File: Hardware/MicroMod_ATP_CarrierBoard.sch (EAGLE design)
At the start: 68 parts, among them J19 QWIIC_RIGHT_ANGLE, J2 JTAG, J20 QWIIC_RIGHT_ANGLE, J21 1X04_SMD_STRAIGHT_COMBO, J4 USB_A_SMT_FEMALE, J6 MICROMOD-2222-C, J8 1X04_SMD_STRAIGHT_COMBO, U5 AP7361C-33

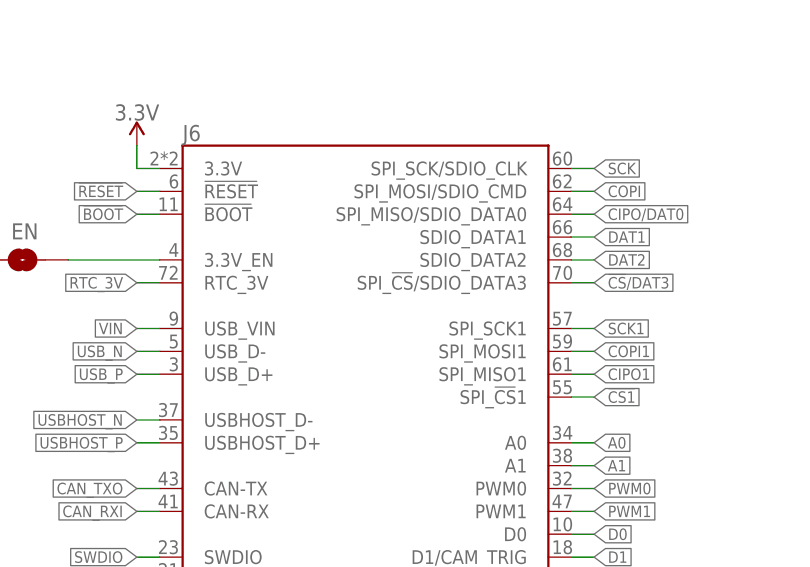
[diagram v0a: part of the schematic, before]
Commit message: Update M.2 Connector and repanelizes for production
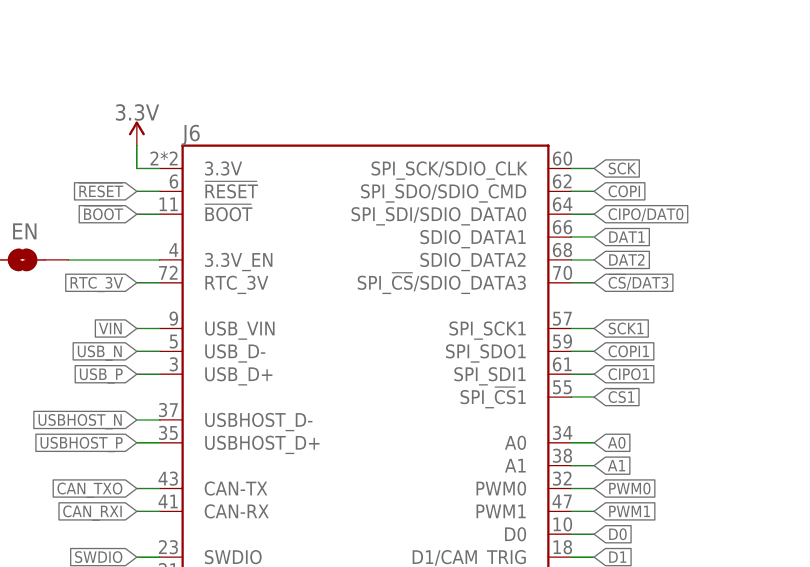
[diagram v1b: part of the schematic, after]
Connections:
- net CIPO/DAT0: now also J6.SPI_SDI/SDIO_DATA0; no longer J6.SPI_MISO/SDIO_DATA0
- net CIPO1: now also J6.SPI_SDI1; no longer J6.SPI_MISO1
- net COPI: now also J6.SPI_SDO/SDIO_CMD; no longer J6.SPI_MOSI/SDIO_CMD
- net COPI1: now also J6.SPI_SDO1; no longer J6.SPI_MOSI1
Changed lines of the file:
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@@
 <wire x1="78.74" y1="129.54" x2="81.28" y2="129.54" width="0.1524" layer="91"/>
 <label x="81.28" y="129.54" size="1.27" layer="95" xref="yes"/>
-<pinref part="J6" gate="J1" pin="SPI_MOSI/SDIO_CMD"/>
+<pinref part="J6" gate="J1" pin="SPI_SDO/SDIO_CMD"/>
 </segment>
 <segment>
@@
 <wire x1="78.74" y1="127" x2="81.28" y2="127" width="0.1524" layer="91"/>
 <label x="81.28" y="127" size="1.27" layer="95" xref="yes"/>
-<pinref part="J6" gate="J1" pin="SPI_MISO/SDIO_DATA0"/>
+<pinref part="J6" gate="J1" pin="SPI_SDI/SDIO_DATA0"/>
 </segment>
 <segment>
@@
 <wire x1="78.74" y1="111.76" x2="81.28" y2="111.76" width="0.1524" layer="91"/>
 <label x="81.28" y="111.76" size="1.27" layer="95" xref="yes"/>
-<pinref part="J6" gate="J1" pin="SPI_MOSI1"/>
+<pinref part="J6" gate="J1" pin="SPI_SDO1"/>
 </segment>
 <segment>
@@
 <wire x1="78.74" y1="109.22" x2="81.28" y2="109.22" width="0.1524" layer="91"/>
 <label x="81.28" y="109.22" size="1.27" layer="95" xref="yes"/>
-<pinref part="J6" gate="J1" pin="SPI_MISO1"/>
-</segment>
-<segment>
+<pinref part="J6" gate="J1" pin="SPI_SDI1"/>
+</segment>
+<segment>

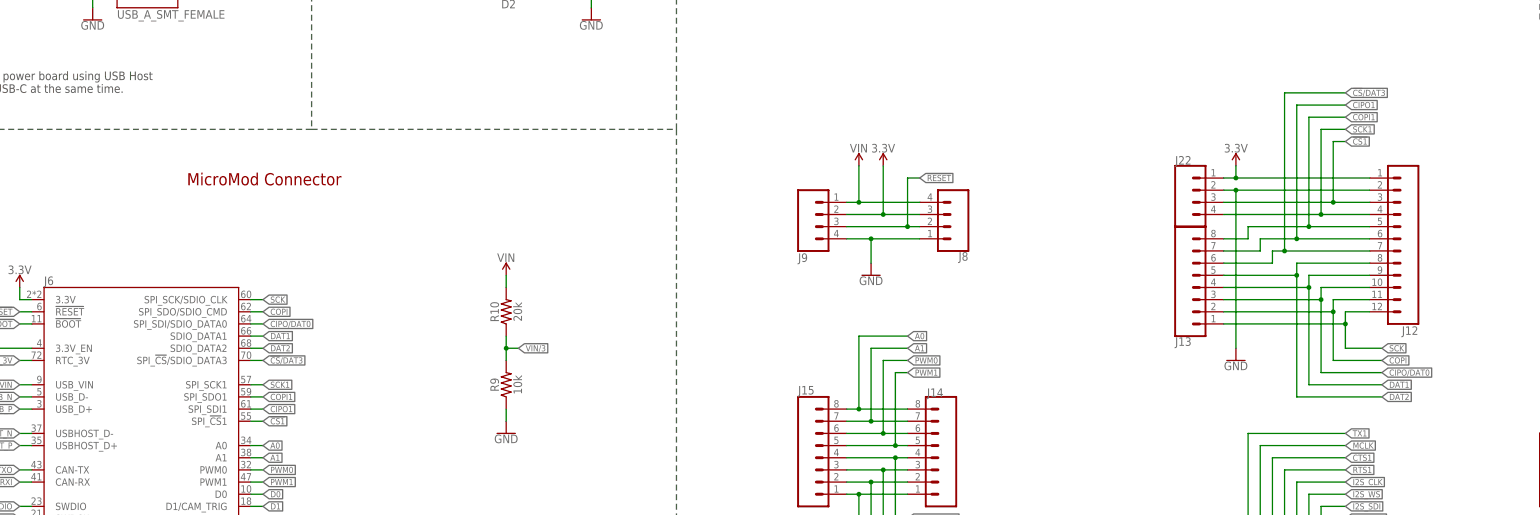
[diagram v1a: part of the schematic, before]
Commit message: Updates micromod female connector and renames nets
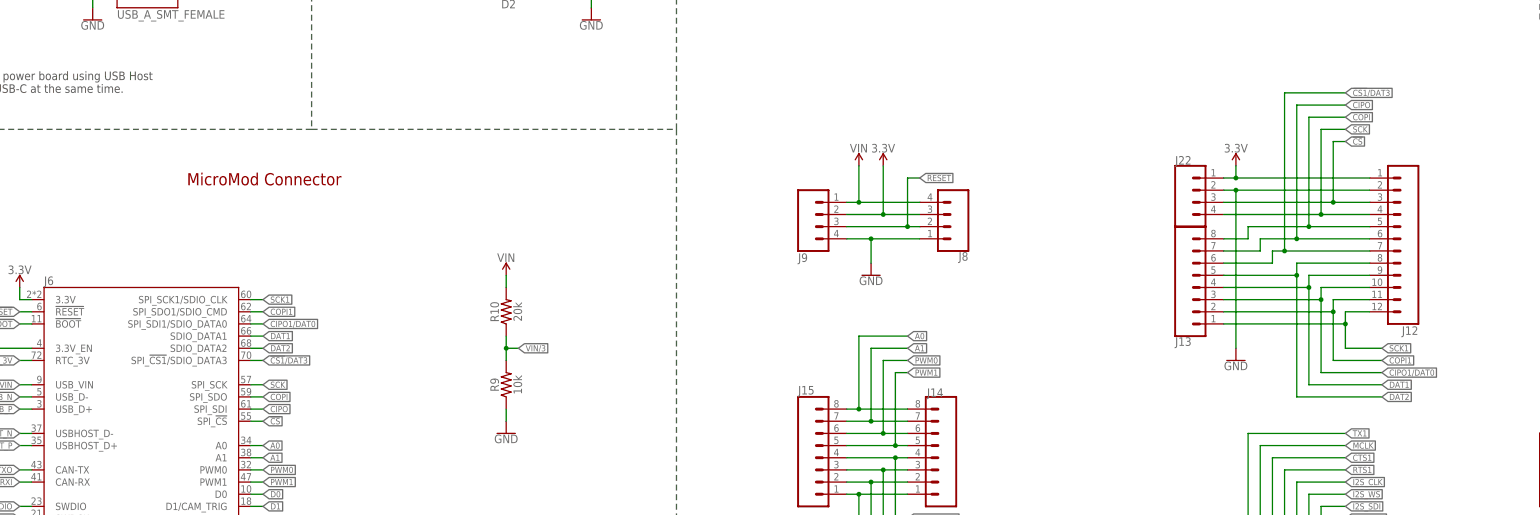
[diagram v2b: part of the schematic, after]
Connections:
- removed net !CS!/DAT3: J12.7, J13.6, J6.SPI_!CS!/SDIO_DATA3
- removed net !CS1: J12.3, J22.3, J6.SPI_!CS!1
- removed net CIPO/DAT0: J12.10, J13.3, J6.SPI_SDI/SDIO_DATA0
- removed net CIPO1: J12.6, J13.7, J6.SPI_SDI1
- new net !CS!: J12.3, J22.3, J6.SPI_!CS!
- new net !CS1!/DAT3: J12.7, J13.6, J6.SPI_!CS1!/SDIO_DATA3
- new net CIPO: J12.6, J13.7, J6.SPI_SDI
- new net CIPO1/DAT0: J12.10, J13.3, J6.SPI_SDI1/SDIO_DATA0
- net COPI: now also J12.5, J13.8, J6.SPI_SDO; no longer J12.11, J13.2, J6.SPI_SDO/SDIO_CMD
- net COPI1: now also J12.11, J13.2, J6.SPI_SDO1/SDIO_CMD; no longer J12.5, J13.8, J6.SPI_SDO1
- net SCK: now also J12.4, J22.4, J6.SPI_SCK; no longer J12.12, J13.1, J6.SPI_SCK/SDIO_CLK
- net SCK1: now also J12.12, J13.1, J6.SPI_SCK1/SDIO_CLK; no longer J12.4, J22.4, J6.SPI_SCK1

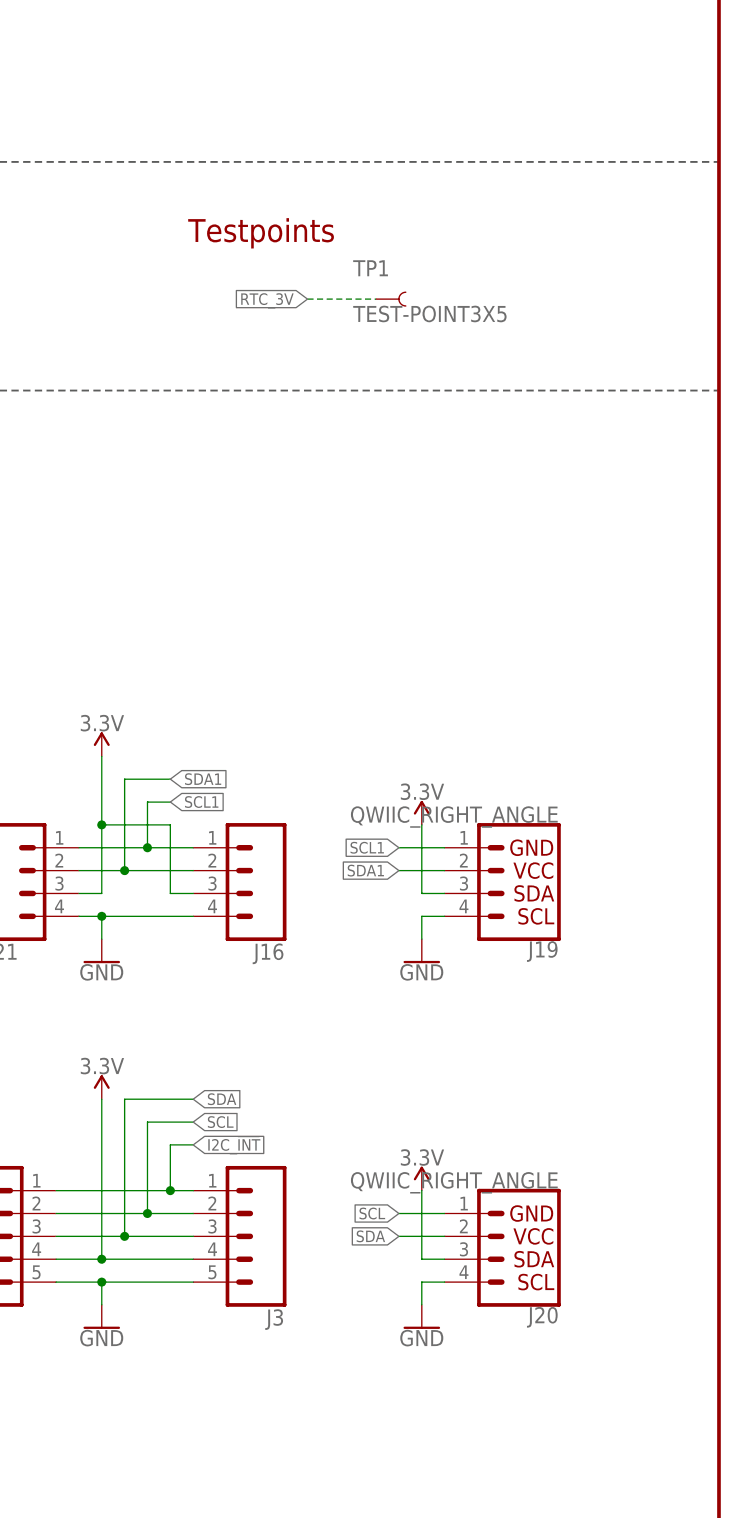
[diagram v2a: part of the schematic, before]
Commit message: Updates silk, fixes Qwiic connector wiring
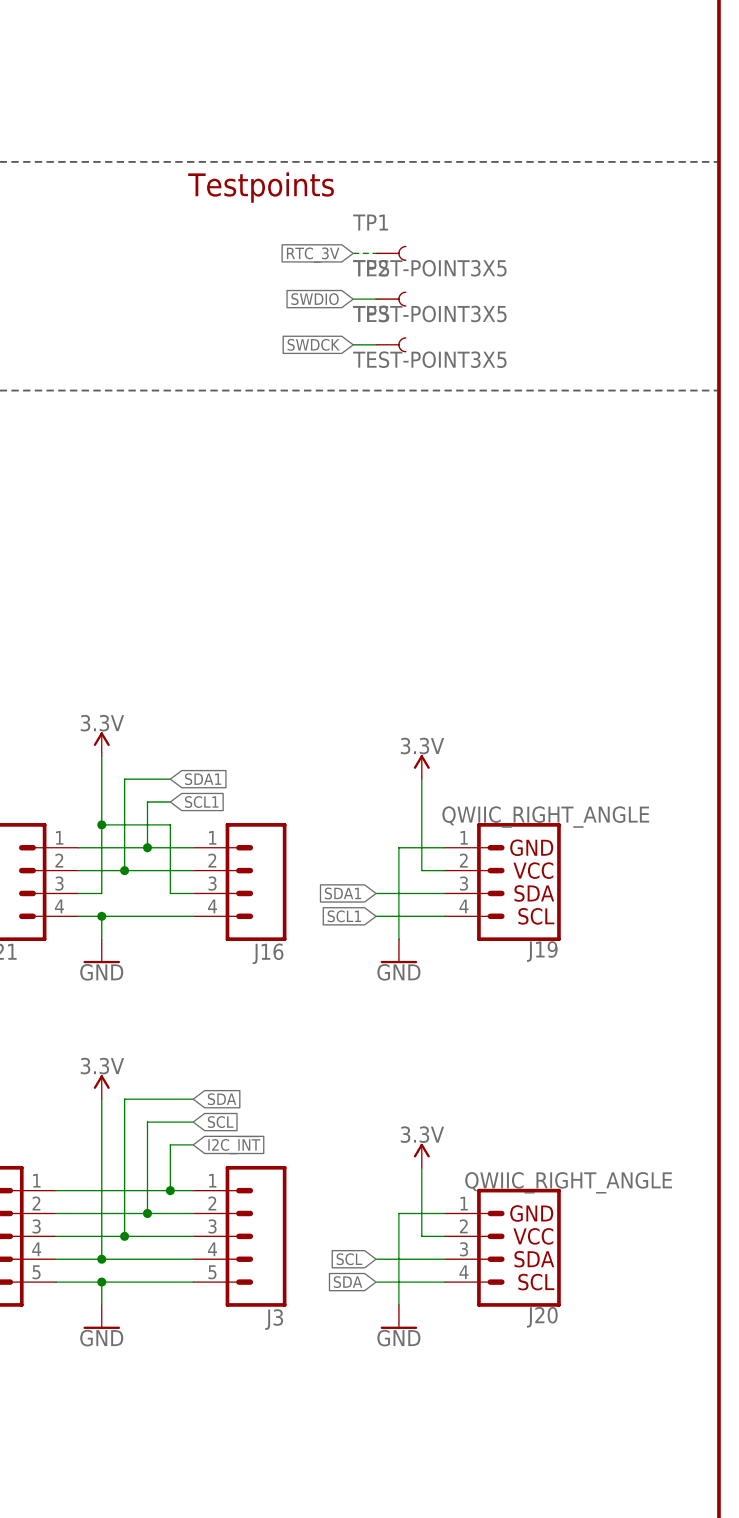
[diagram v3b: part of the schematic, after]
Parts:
- added TP2, TP3: TEST-POINT3X5, SparkFun-Connectors:TEST-POINT3X5
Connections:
- net 3.3V: now also J19.2, J20.2; no longer J19.3, J20.3
- net GND: now also J19.1, J20.1; no longer J19.4, J20.4
- net SCL: now also J20.3; no longer J20.1
- net SCL1: now also J19.4; no longer J19.1
- net SDA: now also J20.4; no longer J20.2
- net SDA1: now also J19.3; no longer J19.2
- net SWDCK: now also TP3.1
- net SWDIO: now also TP2.1
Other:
- moved on the sheet: TP1

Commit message: Updates production files
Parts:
- removed TP2, TP3: TEST-POINT3X5, SparkFun-Connectors:TEST-POINT3X5
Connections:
- net !CS! renamed !CS
- net 3.3V: now also J19.3, J20.3; no longer J19.2, J20.2
- net GND: now also J19.4, J20.4; no longer J19.1, J20.1
- net SCL: now also J20.1; no longer J20.3
- net SCL1: now also J19.1; no longer J19.4
- net SDA: now also J20.2; no longer J20.4
- net SDA1: now also J19.2; no longer J19.3
- net SWDCK: no longer TP3.1
- net SWDIO: no longer TP2.1
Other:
- moved on the sheet: TP1

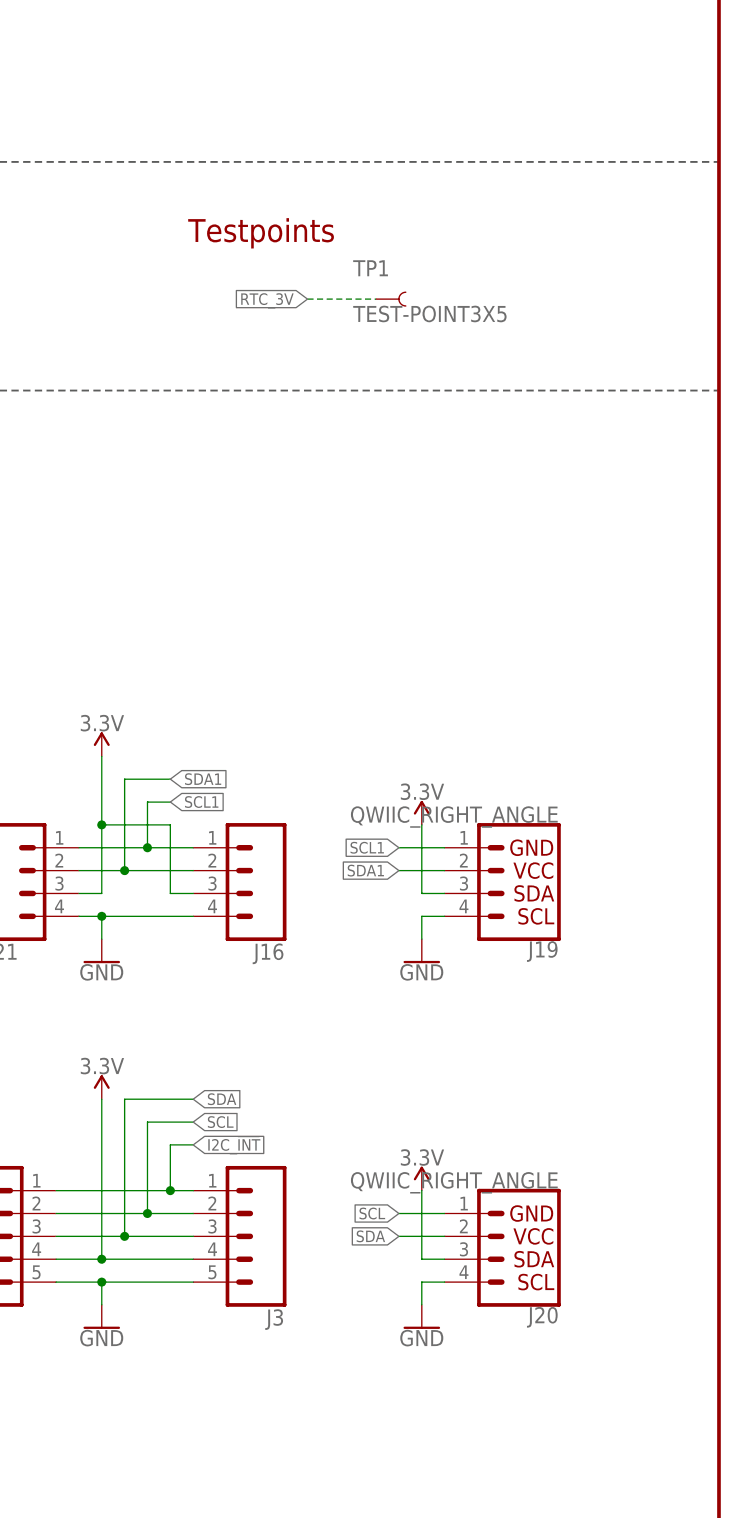
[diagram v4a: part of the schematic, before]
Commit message: Revert "Updates production files"
This reverts commit 213e6b1cbeb41024665e9e154624d95cc9d0b3ef.
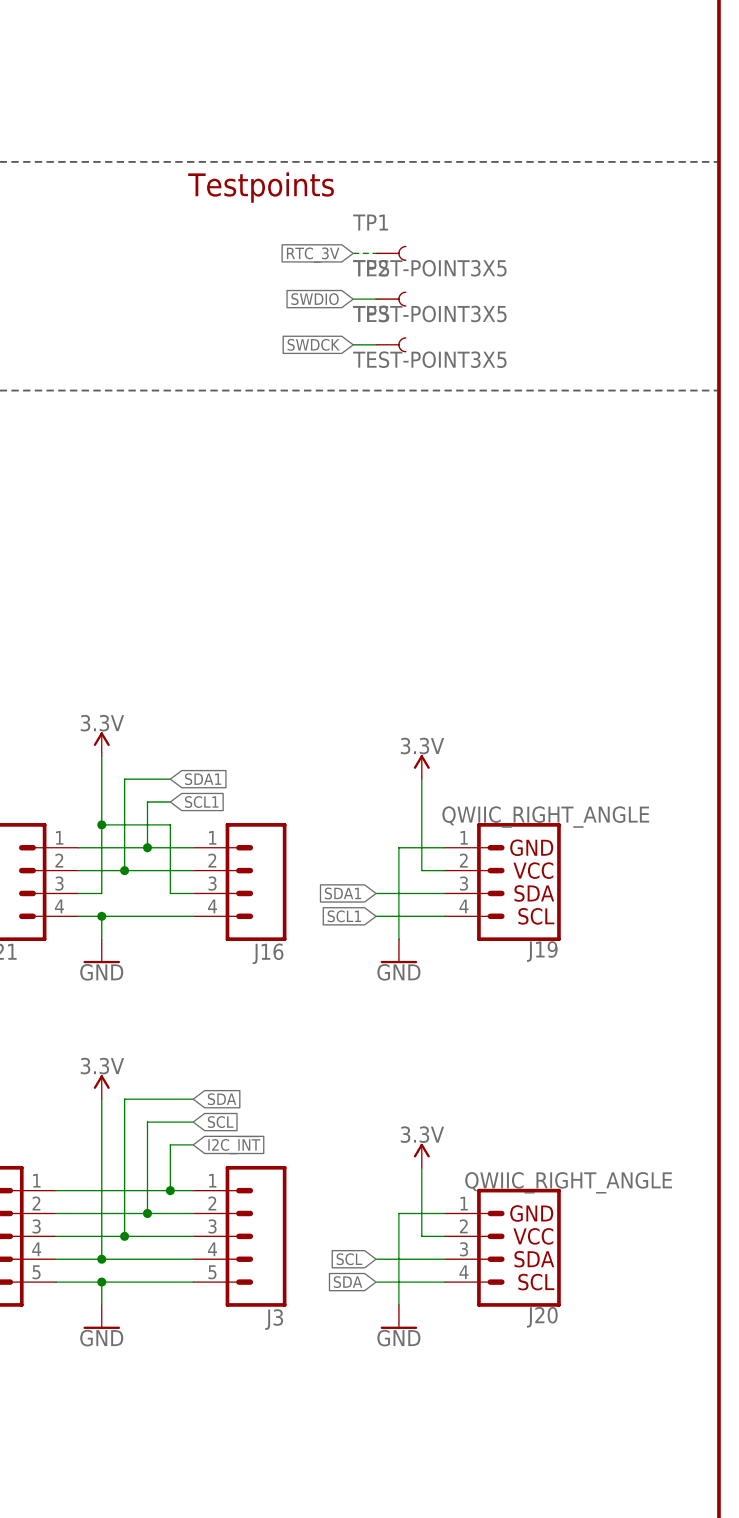
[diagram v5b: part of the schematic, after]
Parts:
- added TP2, TP3: TEST-POINT3X5, SparkFun-Connectors:TEST-POINT3X5
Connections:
- net !CS renamed !CS!
- net 3.3V: now also J19.2, J20.2; no longer J19.3, J20.3
- net GND: now also J19.1, J20.1; no longer J19.4, J20.4
- net SCL: now also J20.3; no longer J20.1
- net SCL1: now also J19.4; no longer J19.1
- net SDA: now also J20.4; no longer J20.2
- net SDA1: now also J19.3; no longer J19.2
- net SWDCK: now also TP3.1
- net SWDIO: now also TP2.1
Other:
- moved on the sheet: TP1
